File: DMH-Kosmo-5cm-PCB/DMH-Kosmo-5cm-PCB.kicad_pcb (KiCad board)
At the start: 2 copper layers, 48 x 175 mm, 0 parts

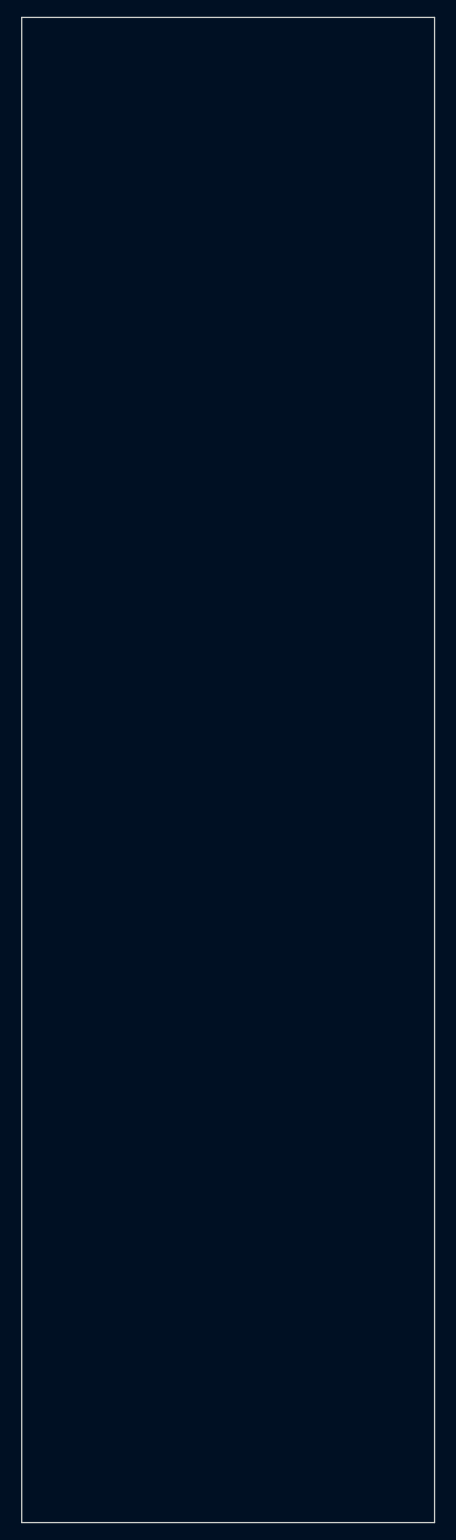
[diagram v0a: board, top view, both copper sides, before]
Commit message: Enlarged PCB limits
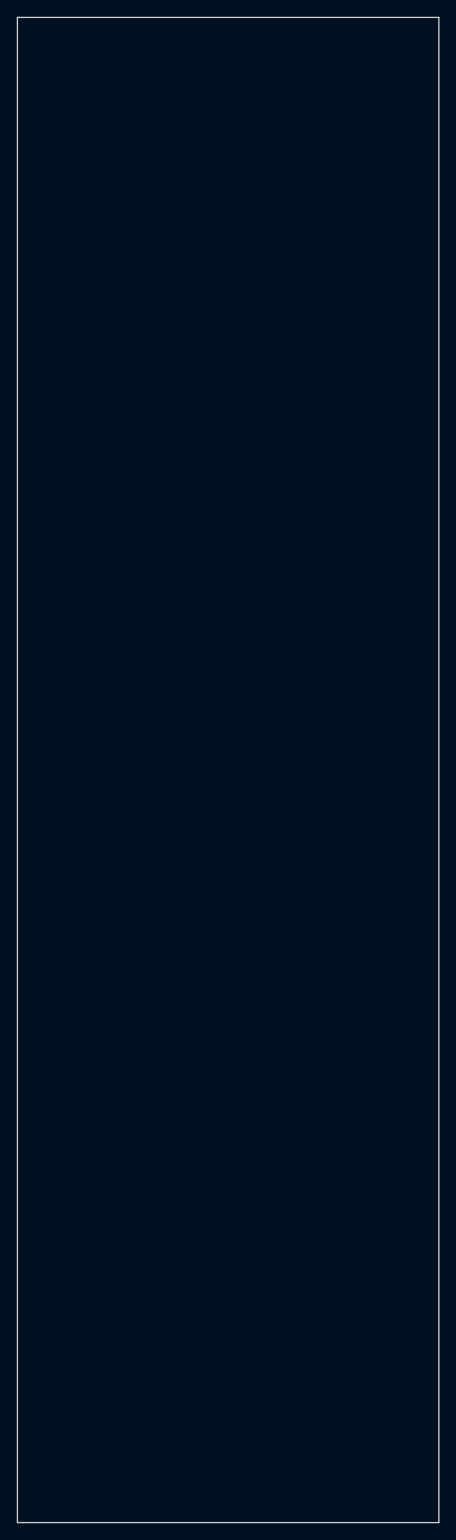
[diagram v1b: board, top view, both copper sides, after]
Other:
- board size 48 x 175 mm -> 49 x 175 mm
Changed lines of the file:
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@@
 	)
 	(gr_rect
-		(start 51 42.5)
-		(end 99 217.5)
+		(start 50.5 42.5)
+		(end 99.5 217.5)
 		(stroke
 			(width 0.05)
